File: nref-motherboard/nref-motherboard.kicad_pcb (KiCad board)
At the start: 6 copper layers, 110 x 80 mm, 197 parts, among them J1 POWSW, J10 DISP, J11 BAT1, J12 BAT2, J13 SYSCTL_USB, J16 Conn_01x10_Pin, J17 Conn_01x10_Pin, J18 Conn_01x20, J19 SER, J2 Conn_01x12_Pin, J3 USBSEL, J4 1-2199230-6, J5 SYSCTL, J6 USB_INT1, J7 PWR, J8 Conn_01x12_Pin, J9 Conn_01x14_Pin, Q1 NTMFD6H840NL, Q2 NTMFD6H840NL, SW1 SW_DIP_x01, SW2 RESET, SW3 SW_DIP_x01, U1 reform2-som-connector, U10 BQ25756RRVR, U11 LM62460, U2 74HC573, U3 MAX1837EUT33+T, U4 USB2412-DZK, U5 LM62460, U6 USB2412-DZK, U8 RP2040, U9 W25Q32JVSS, Y1 12MHz 18pF, Y2 24MHz, Y3 24MHz

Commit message: motherboard: continue design; almost feature complete
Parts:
- removed C74, C75, C76, C77, C78, C79: 0.1uF, Capacitor_SMD:C_0402_1005Metric
- removed R45, R46, R47, R48, R49, R50, R66, R70: 0, Resistor_SMD:R_0402_1005Metric
- removed R65, R69: 50k, Resistor_SMD:R_0402_1005Metric
- removed R67: 12k 1%, Resistor_SMD:R_0402_1005Metric
- removed R68: 1M, Resistor_SMD:R_0402_1005Metric
- removed TP1, TP2: TestPoint, TestPoint:TestPoint_Pad_D1.0mm
- removed U4, U6: USB2412-DZK, footprints:QFN50P500X500X100-29N
- removed Y3: 24MHz, Crystal:Crystal_SMD_3225-4Pin_3.2x2.5mm
- added D2: D_Small, Diode_SMD:D_0603_1608Metric, F.Cu at (74.7, 105.6)
- added D3: D_Small, Diode_SMD:D_0603_1608Metric, F.Cu at (76.3, 105.6)
- added D8: D_Small, Diode_SMD:D_0603_1608Metric, F.Cu at (57.9, 120.3)
- added D9: D_Small, Diode_SMD:D_0603_1608Metric, F.Cu at (55.2, 120.3)
- added H2: MountingHole_Pad, MountingHole:MountingHole_2.2mm_M2_Pad, F.Cu at (143.3, 155.1)
- added H3: MountingHole_Pad, MountingHole:MountingHole_2.2mm_M2_Pad, F.Cu at (143.3, 119.1)
- added H4: MountingHole_Pad, MountingHole:MountingHole_2.2mm_M2_Pad, F.Cu at (26.7, 155.1)
- added H5: MountingHole_Pad, MountingHole:MountingHole_2.2mm_M2_Pad, F.Cu at (26.7, 119.1)
- added U7: USB2514B_Bi, Package_DFN_QFN:QFN-36-1EP_6x6mm_P0.5mm_EP3.7x3.7mm, F.Cu at (111.6, 118.1)
- C72, C73: value 18pF -> 0.1uF
- R15: value 0 -> 50k
- R64: value 50k -> 0
- moved J6 117.5 mm to (143.0, 125.5), turned to 90 degrees
- moved J19 117.5 mm to (143.0, 134.3), turned to 90 degrees
- moved C72 50.5 mm to (117.1, 119.0)
- moved C73 50.5 mm to (117.1, 121.0)
- moved R64 48.9 mm to (117.1, 117.0)
- moved J1 48.8 mm to (32.8, 168.1)
- moved Y2 47.0 mm to (124.7, 126.3)
- moved R15 46.6 mm to (117.1, 115.0)
- moved C15 40.9 mm to (123.8, 113.5)
- moved C17 40.9 mm to (123.8, 115.5)
- moved C64 40.9 mm to (123.8, 117.5)
- moved C65 40.9 mm to (123.8, 119.4)
- moved R22 40.9 mm to (121.0, 127.4)
- moved R34 40.9 mm to (121.0, 129.4)
- moved R35 40.9 mm to (123.9, 121.4)
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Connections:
- C72 pad 1: Net-(U6-XTALOUT) -> +3V3
- C73 pad 1: Net-(U6-XTALIN/CLKIN) -> +3V3
- J3 pad 1: USB2B_DN -> USB2C_DN
- J3 pad 2: USB2B_DP -> USB2C_DP
- J4 pad 11: Net-(J4-Pad11) -> GND
- J4 pad 13: Net-(J4-Pad13) -> GND
- J4 pad 23: Net-(J4-Pad23) -> GND
- J4 pad 25: Net-(J4-Pad25) -> GND
- J4 pad 29: unconnected-(J4-Pad29) -> PCIE1_RX2_N
- J4 pad 31: unconnected-(J4-Pad31) -> PCIE1_RX2_P
- J4 pad 35: Net-(J4-Pad35) -> PCIE1_TX2_N
- J4 pad 37: Net-(J4-Pad37) -> PCIE1_TX2_P
- J6 pad 2: USB1B_DN -> USB2B_DN
- J6 pad 3: USB1B_DP -> USB2B_DP
- J8 pad 11: USB1A_DP -> USB1_DP
- J8 pad 12: USB1A_DN -> USB1_DN
- R15 pad 1: USB_HUB_RESET -> GND
- R42 pad 1: Net-(U4-VBUS_DET) -> +3V3
- R42 pad 2: +3V3 -> Net-(U7-VBUS_DET)
- R64 pad 1: GND -> Net-(U1-QSPIA_DATA2)
- R64 pad 2: Net-(U6-HS_IND) -> GND
- U1 pad 82: unconnected-(U1-QSPIA_DATA4-Pad82) -> PCIE2_RX2_P
- U1 pad 84: unconnected-(U1-QSPIA_DATA3-Pad84) -> PCIE2_RX2_N
- U1 pad 86: unconnected-(U1-QSPIA_DATA2-Pad86) -> Net-(U1-QSPIA_DATA2)
- U1 pad 88: unconnected-(U1-QSPIA_DATA1-Pad88) -> PCIE2_TX2_P
- U1 pad 90: unconnected-(U1-QSPIA_DATA0-Pad90) -> PCIE2_TX2_N
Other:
- board size 110 x 80 mm -> 122.6 x 80 mm

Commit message: motherboard: some initial routing, mostly power
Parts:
- J11, J12: footprint Connector_JST:JST_SH_SM06B-SRSS-TB_1x06-1MP_P1.00mm_Horizontal -> Connector_JST:JST_SH_SM07B-SRSS-TB_1x07-1MP_P1.00mm_Horizontal
- moved R62 26.8 mm to (36.9, 146.0)
- moved R63 20.5 mm to (36.9, 134.8), turned to -90 degrees
- moved SW1 15.7 mm to (81.5, 102.0), turned to 180 degrees
- moved D7 13.1 mm to (38.8, 120.6), turned to 90 degrees
- moved R25 9.24 mm to (38.7, 134.2), turned to 90 degrees
- moved SW2 8.24 mm to (73.2, 110.1)
- moved R38 7.81 mm to (84.3, 110.7)
- moved R40 7.81 mm to (84.3, 109.7)
- moved R41 7.81 mm to (84.3, 108.7)
- moved D5 7.81 mm to (81.7, 109.7)
- moved R54 7.35 mm to (44.9, 114.2), turned to -90 degrees
- moved R7 6.64 mm to (49.7, 113.4), turned to 0 degrees
- moved C12 6.47 mm to (66.3, 111.9), turned to 90 degrees
- moved C41 6.27 mm to (45.7, 110.9), turned to 90 degrees
- moved R10 5.74 mm to (45.9, 114.2), turned to 90 degrees
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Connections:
- J11 pad 3: BAT1_SCL -> BAT1_ALERT
- J11 pad 5: BAT1_V+ -> BAT1_SCL
- J11 pad 6: GND -> BAT1_V+
- J12 pad 3: BAT2_SCL -> BAT2_ALERT
- J12 pad 4: BAT2_SDA -> BAT2_SCL
- J12 pad 5: BAT2_V+ -> BAT2_SDA
- J12 pad 6: GND -> BAT2_V+
- J4 pad 11: GND -> PCIE2_TX4_N
- J4 pad 13: GND -> PCIE2_TX4_P
- J4 pad 17: unconnected-(J4-Pad17) -> PCIE2_RX3_N
- J4 pad 19: unconnected-(J4-Pad19) -> PCIE2_RX3_P
- J4 pad 23: GND -> PCIE2_TX3_N
- J4 pad 25: GND -> PCIE2_TX3_P
- J4 pad 29: PCIE1_RX2_N -> PCIE2_RX2_N
- J4 pad 31: PCIE1_RX2_P -> PCIE2_RX2_P
- J4 pad 35: PCIE1_TX2_N -> PCIE2_TX2_N
- J4 pad 37: PCIE1_TX2_P -> PCIE2_TX2_P
- J4 pad 41: PCIE1_RX_N -> PCIE2_RX_N
- J4 pad 43: PCIE1_RX_P -> PCIE2_RX_P
- J4 pad 47: PCIE1_TX_N -> PCIE2_TX_N
- J4 pad 49: PCIE1_TX_P -> PCIE2_TX_P
- J4 pad 5: unconnected-(J4-Pad5) -> PCIE2_RX4_N
- J4 pad 53: PCIE1_CLK_N -> PCIE2_CLK_N
- J4 pad 55: PCIE1_CLK_P -> PCIE2_CLK_P
- J4 pad 7: unconnected-(J4-Pad7) -> PCIE2_RX4_P
- R43 pad 2: PCIE1_CLK_P -> PCIE2_CLK_P
- R44 pad 2: PCIE1_CLK_N -> PCIE2_CLK_N
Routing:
- net ETH0_D-: track 0.00 -> 78.7 mm, vias 0 -> 2
- net ETH0_D+: track 0.00 -> 78.7 mm, vias 0 -> 2
- net ETH0_C+: track 0.00 -> 78.6 mm, vias 0 -> 2
- net ETH0_C-: track 0.00 -> 78.6 mm, vias 0 -> 2
- net ETH0_B-: track 0.00 -> 78.5 mm, vias 0 -> 2
- net ETH0_B+: track 0.00 -> 78.5 mm, vias 0 -> 2
- net ETH0_A+: track 0.00 -> 78.3 mm, vias 0 -> 2
- net ETH0_A-: track 0.00 -> 78.3 mm, vias 0 -> 2
- net VCC: track 0.00 -> 71.3 mm
- net GND: track 0.00 -> 67.8 mm, vias 0 -> 41
- net VPD: track 0.00 -> 36.5 mm
- net +5V: track 0.00 -> 25.0 mm
- net /SW1: track 0.00 -> 24.8 mm
- net /SW2: track 0.00 -> 21.8 mm, vias 0 -> 2
- net /DRV_SUP: track 0.00 -> 13.8 mm, vias 0 -> 2
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- added copper zone on B.Cu, net GND
- added copper zone on F.Cu, net GND
- added copper zone on In1.Cu, net GND
- added copper zone on In2.Cu, net GND
- added copper zone on In3.Cu, net GND
- added copper zone on In4.Cu, net GND

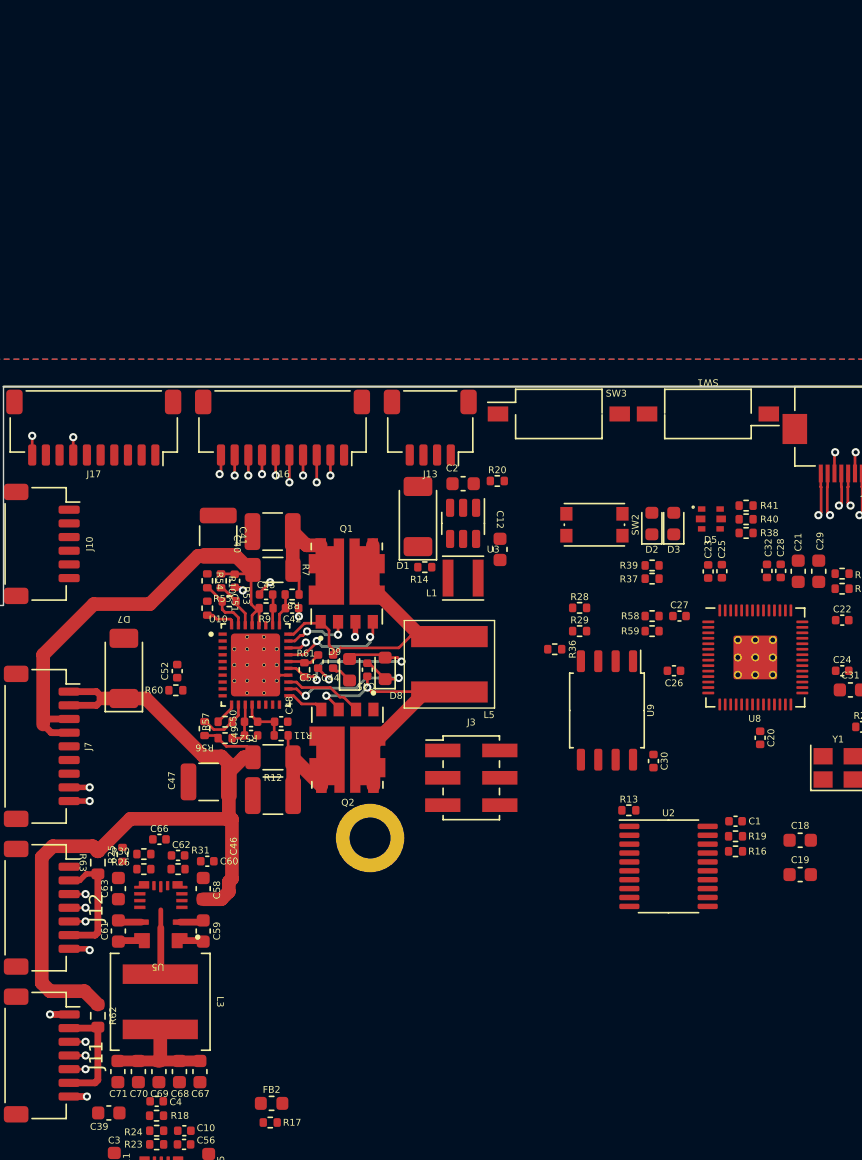
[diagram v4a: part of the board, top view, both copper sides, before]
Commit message: motherboard: consolidate switches and jumpers into one 8x1.27mm dip, liion/lifepo switch
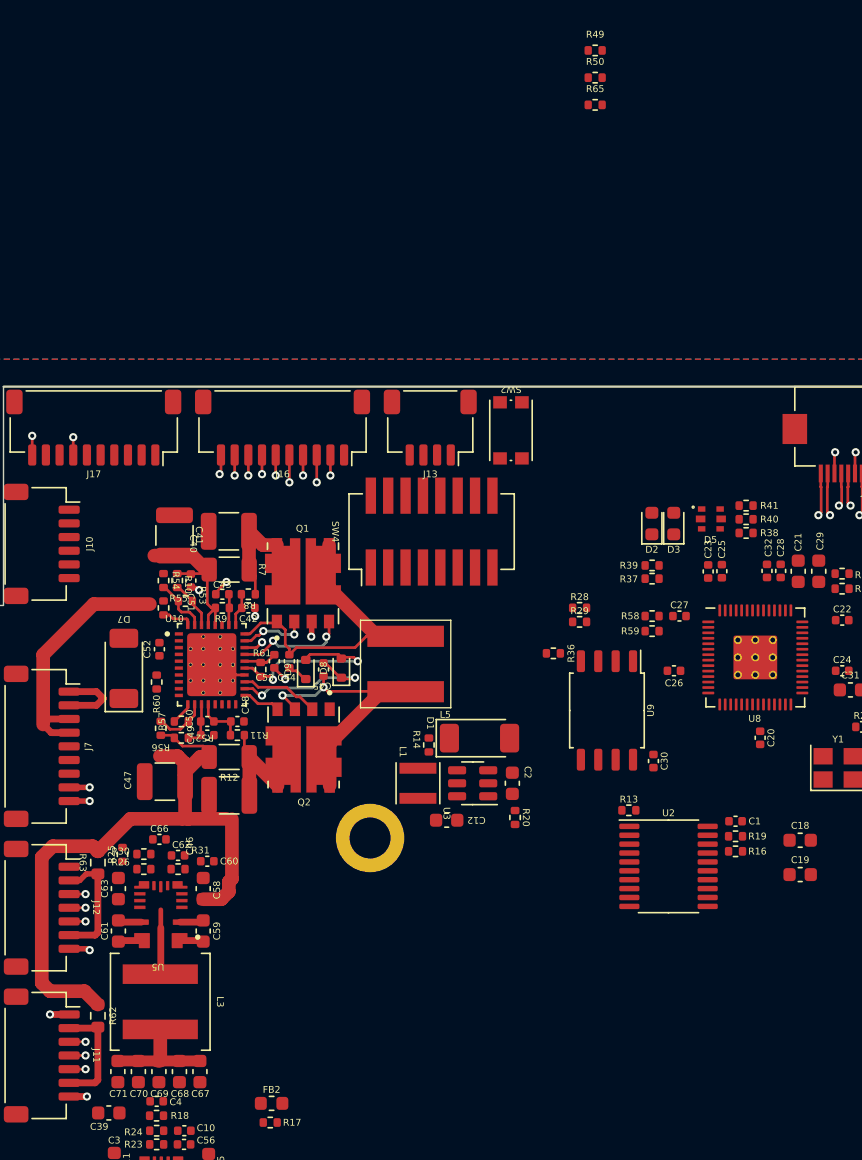
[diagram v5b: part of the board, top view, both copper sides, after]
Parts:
- removed J3: USBSEL, Connector_PinHeader_2.00mm:PinHeader_2x03_P2.00mm_Vertical_SMD
- removed SW1, SW3: SW_DIP_x01, Button_Switch_SMD:SW_DIP_SPSTx01_Slide_Omron_A6S-110x_W8.9mm_P2.54mm
- added R49: 4.7k, Resistor_SMD:R_0402_1005Metric, F.Cu at (73.3, 75.4)
- added R50: 4.7k, Resistor_SMD:R_0402_1005Metric, F.Cu at (73.3, 77.4)
- added R65: 20k, Resistor_SMD:R_0402_1005Metric, F.Cu at (73.3, 79.4)
- added SW4: SW_DIP_x08, Button_Switch_SMD:SW_DIP_SPSTx08_Slide_KingTek_DSHP08TJ_W5.25mm_P1.27mm_JPin, F.Cu at (61.3, 110.6)
- D8, D9: value D_Small -> SBR1A20T5-7; footprint Diode_SMD:D_0603_1608Metric -> Diode_SMD:D_SOD-523
- R53: value 73.2k -> DNP
- R57: value 24.88k -> 29.8k
- R58, R59: value R_Small -> 10k
- moved R20 24.6 mm to (67.4, 131.5), turned to -90 degrees
- moved C2 22.2 mm to (67.2, 129.0), turned to -90 degrees
- moved C12 20.2 mm to (62.4, 131.7), turned to 0 degrees
- moved U3 19.0 mm to (64.3, 129.0), turned to 180 degrees
- moved D1 16.8 mm to (64.8, 125.7), turned to 0 degrees
- moved L1 15.4 mm to (60.3, 129.0), turned to -90 degrees
- moved R14 13.0 mm to (61.1, 126.2), turned to -90 degrees
- moved SW2 9.21 mm to (67.1, 103.2), turned to -90 degrees
- moved C41 3.20 mm to (42.5, 110.9)
- moved C42 3.20 mm to (47.9, 116.2)
- moved C43 3.20 mm to (46.0, 115.2)
- moved C44 3.20 mm to (50.9, 120.1)
- moved C45 3.20 mm to (53.4, 120.7)
- moved C46 3.20 mm to (46.5, 129.9)
- moved C47 3.20 mm to (41.8, 128.9)
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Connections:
- net /FB renamed CHRG_LIION_A
- net BAT1_SCL renamed Net-(J11-Pin_5)
- net BAT1_SDA renamed Net-(J11-Pin_4)
- net BAT2_SCL renamed Net-(J12-Pin_4)
- net BAT2_SDA renamed Net-(J12-Pin_5)
- net Net-(D2-A) renamed PWR_OVERRIDE
- U10 pad 3: unconnected-(U10-~{INT}-Pad3) -> CHRG_ALERT
- U8 pad 29: MODEM_PWROFFn -> CHRG_ALERT
- U8 pad 31: MODEM_RESET_3V3 -> unconnected-(U8-GPIO20-Pad31)
- U8 pad 39: PHONE_DPR_3V3 -> unconnected-(U8-GPIO27_ADC1-Pad39)
- U8 pad 4: ~{DISP_RESET} -> RP_SDA1
- U8 pad 5: RP_FLIGHTMODE -> RP_SCL1
- U8 pad 8: WOWWAN_3V3 -> BAT1_ALERT
- U8 pad 9: DISP_EN -> BAT2_ALERT
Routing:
- net VCC: track 71.3 -> 62.2 mm
- net VPD: track 36.5 -> 31.5 mm

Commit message: lots of motherboard routing
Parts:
- added C75: 10uF, Capacitor_SMD:C_0603_1608Metric, F.Cu at (114.8, 134.2)
- added D10: LED_RED, LED_SMD:LED_0603_1608Metric, F.Cu at (38.5, 111.3)
- added D11: LED_RED, LED_SMD:LED_0603_1608Metric, F.Cu at (38.5, 109.7)
- added D4: LED_RED, LED_SMD:LED_0402_1005Metric, F.Cu at (55.3, 151.6)
- added R45: 0, Resistor_SMD:R_0402_1005Metric, F.Cu at (49.4, 140.3)
- added R46: 0, Resistor_SMD:R_0402_1005Metric, F.Cu at (49.4, 142.3)
- added R47: 0, Resistor_SMD:R_0402_1005Metric, F.Cu at (49.4, 144.3)
- added R48: 0, Resistor_SMD:R_0402_1005Metric, F.Cu at (49.4, 146.2)
- added R66: 0, Resistor_SMD:R_0402_1005Metric, F.Cu at (94.2, 166.7)
- added R67: 0, Resistor_SMD:R_0402_1005Metric, F.Cu at (93.1, 166.7)
- added R68: 0, Resistor_SMD:R_0402_1005Metric, F.Cu at (114.8, 132.8)
- added R69: 1M, Resistor_SMD:R_0402_1005Metric, F.Cu at (114.4, 135.6)
- added R70: 5.24k, Resistor_SMD:R_0402_1005Metric, F.Cu at (70.8, 149.1)
- added R71: 10k, Resistor_SMD:R_0402_1005Metric, F.Cu at (58.6, 148.7)
- added R72: 10k, Resistor_SMD:R_0402_1005Metric, F.Cu at (38.6, 113.1)
- added R73: 10k, Resistor_SMD:R_0402_1005Metric, F.Cu at (37.5, 113.1)
- added R74: 10k, Resistor_SMD:R_0402_1005Metric, F.Cu at (58.3, 146.1)
- added R75: 100k, Resistor_SMD:R_0402_1005Metric, F.Cu at (50.8, 137.0)
- added R76: 100k, Resistor_SMD:R_0402_1005Metric, F.Cu at (53.9, 147.7)
- added TH1: 10k, Resistor_SMD:R_0402_1005Metric, F.Cu at (39.1, 124.8)
- R15, R35, R4, R5: value 50k -> 47k
- R60: value 10k -> 30.31k
- R62, R63: value TODO -> 0
- moved J6 100.5 mm to (45.1, 103.0), turned to 180 degrees
- moved J13 87.9 mm to (139.4, 143.1), turned to 90 degrees
- moved J5 58.5 mm to (37.3, 103.0), turned to 180 degrees
- moved R64 51.7 mm to (101.5, 166.2), turned to 90 degrees
- moved R41 50.0 mm to (34.4, 112.7), turned to 90 degrees
- moved R40 49.0 mm to (35.4, 112.7), turned to 90 degrees
- moved R38 47.9 mm to (36.4, 112.7), turned to 90 degrees
- moved R43 47.2 mm to (98.1, 164.3)
- moved D5 46.3 mm to (35.4, 110.4)
- moved R44 45.2 mm to (98.0, 165.4)
- moved R49 42.4 mm to (78.5, 117.5), turned to 180 degrees
- moved R65 39.7 mm to (65.6, 118.3), turned to -90 degrees
- moved R50 39.6 mm to (79.6, 116.5), turned to 180 degrees
- moved SW2 36.1 mm to (32.0, 111.6)
- moved D2 34.9 mm to (60.6, 140.6)
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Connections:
- J4 pad 50: PCIE1_RESETn -> PCIE2_RESETn
- R60 pad 1: Net-(U10-TS) -> GND
- R60 pad 2: GND -> Net-(U10-TS)
- U1 pad 43: unconnected-(U1-CSI_P2_D0_N-Pad43) -> PCIE2_RX3_P
- U1 pad 45: unconnected-(U1-CSI_P2_D0_P-Pad45) -> PCIE2_RX3_N
- U1 pad 49: unconnected-(U1-CSI_P2_D1_N-Pad49) -> PCIE2_TX3_P
- U1 pad 51: unconnected-(U1-CSI_P2_D1_P-Pad51) -> PCIE2_TX3_N
- U1 pad 55: unconnected-(U1-CSI_P2_D2_N-Pad55) -> PCIE2_RX4_P
- U1 pad 57: unconnected-(U1-CSI_P2_D2_P-Pad57) -> PCIE2_RX4_N
- U1 pad 61: unconnected-(U1-CSI_P2_D3_N-Pad61) -> PCIE2_TX4_P
- U1 pad 63: unconnected-(U1-CSI_P2_D3_P-Pad63) -> PCIE2_TX4_N
- U1 pad 67: unconnected-(U1-CSI_P2_CK_N-Pad67) -> PCIE2_CLK2_N
- U1 pad 69: unconnected-(U1-CSI_P2_CK_P-Pad69) -> PCIE2_CLK2_P
- U10 pad 4: unconnected-(U10-STAT1-Pad4) -> CHRG_STAT1
- U10 pad 5: unconnected-(U10-STAT2-Pad5) -> CHRG_STAT2
- U10 pad 6: unconnected-(U10-~{PG}-Pad6) -> ~{CHRG_PG}
- U10 pad 7: unconnected-(U10-~{CE}-Pad7) -> ~{CHRG_CE}
- U11 pad 10: +5V -> Net-(U11-RESET)
- U5 pad 10: +3V3 -> Net-(U5-RESET)
- U7 pad 26: USB_HUB_RESET -> Net-(U7-RESET_N)
- U8 pad 31: unconnected-(U8-GPIO20-Pad31) -> ~{CHRG_CE}
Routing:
- net DAC_BCLK: track 0.00 -> 142.0 mm, vias 0 -> 2
- net DAC_MCLK: track 0.00 -> 136.4 mm, vias 0 -> 2
- net DAC_DIN: track 0.00 -> 135.2 mm, vias 0 -> 2
- net DAC_TXFS: track 0.00 -> 134.5 mm, vias 0 -> 2
- net DAC_DOUT: track 0.00 -> 132.8 mm, vias 0 -> 2
- net GND: track 67.8 -> 173.8 mm, vias 41 -> 94
- net HDMI_HPD: track 0.00 -> 90.8 mm, vias 0 -> 2
- net HDMI_SCL: track 0.00 -> 88.0 mm, vias 0 -> 2
- net HDMI_CEC: track 0.00 -> 87.8 mm, vias 0 -> 2
- net HDMI_SDA: track 0.00 -> 86.2 mm, vias 0 -> 2
- net USB2_TXN: track 0.00 -> 80.3 mm, vias 0 -> 2
- net USB2_RXN: track 0.00 -> 79.8 mm, vias 0 -> 2
- net USB2_TXP: track 0.00 -> 78.7 mm, vias 0 -> 2
- net USB2_RXP: track 0.00 -> 78.4 mm, vias 0 -> 2
- net ETH0_LED_LINK1: track 0.00 -> 76.2 mm, vias 0 -> 2
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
